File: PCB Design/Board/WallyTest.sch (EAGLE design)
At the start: 5 parts, among them IC1 ESP32-S3-WROOM-1-N16

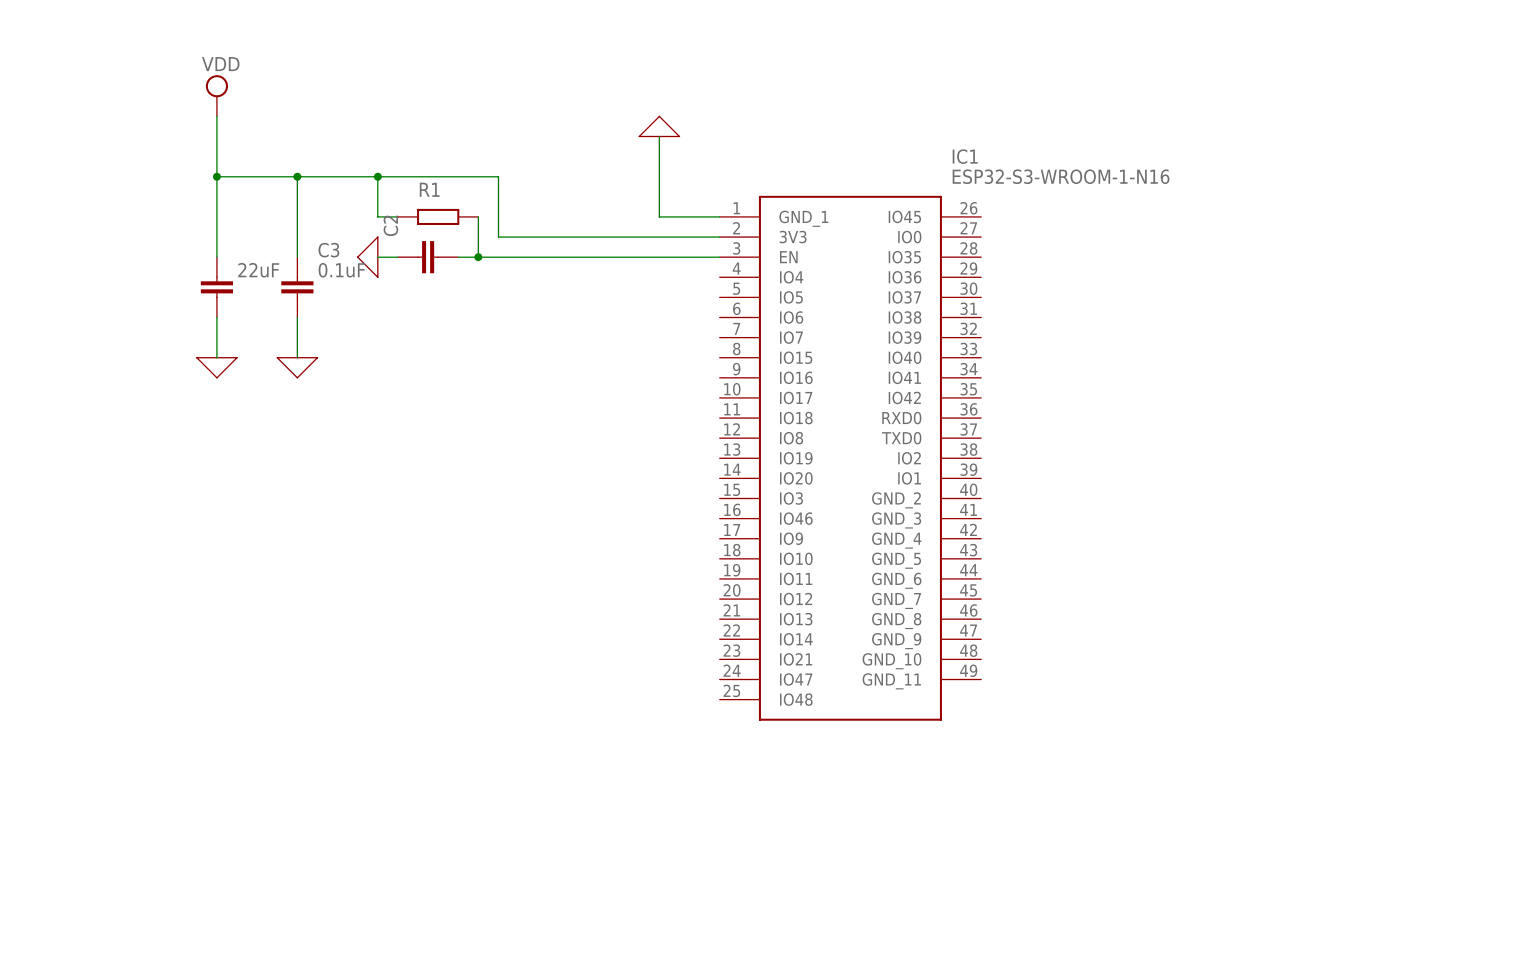
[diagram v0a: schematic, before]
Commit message: wally board with gps and lora
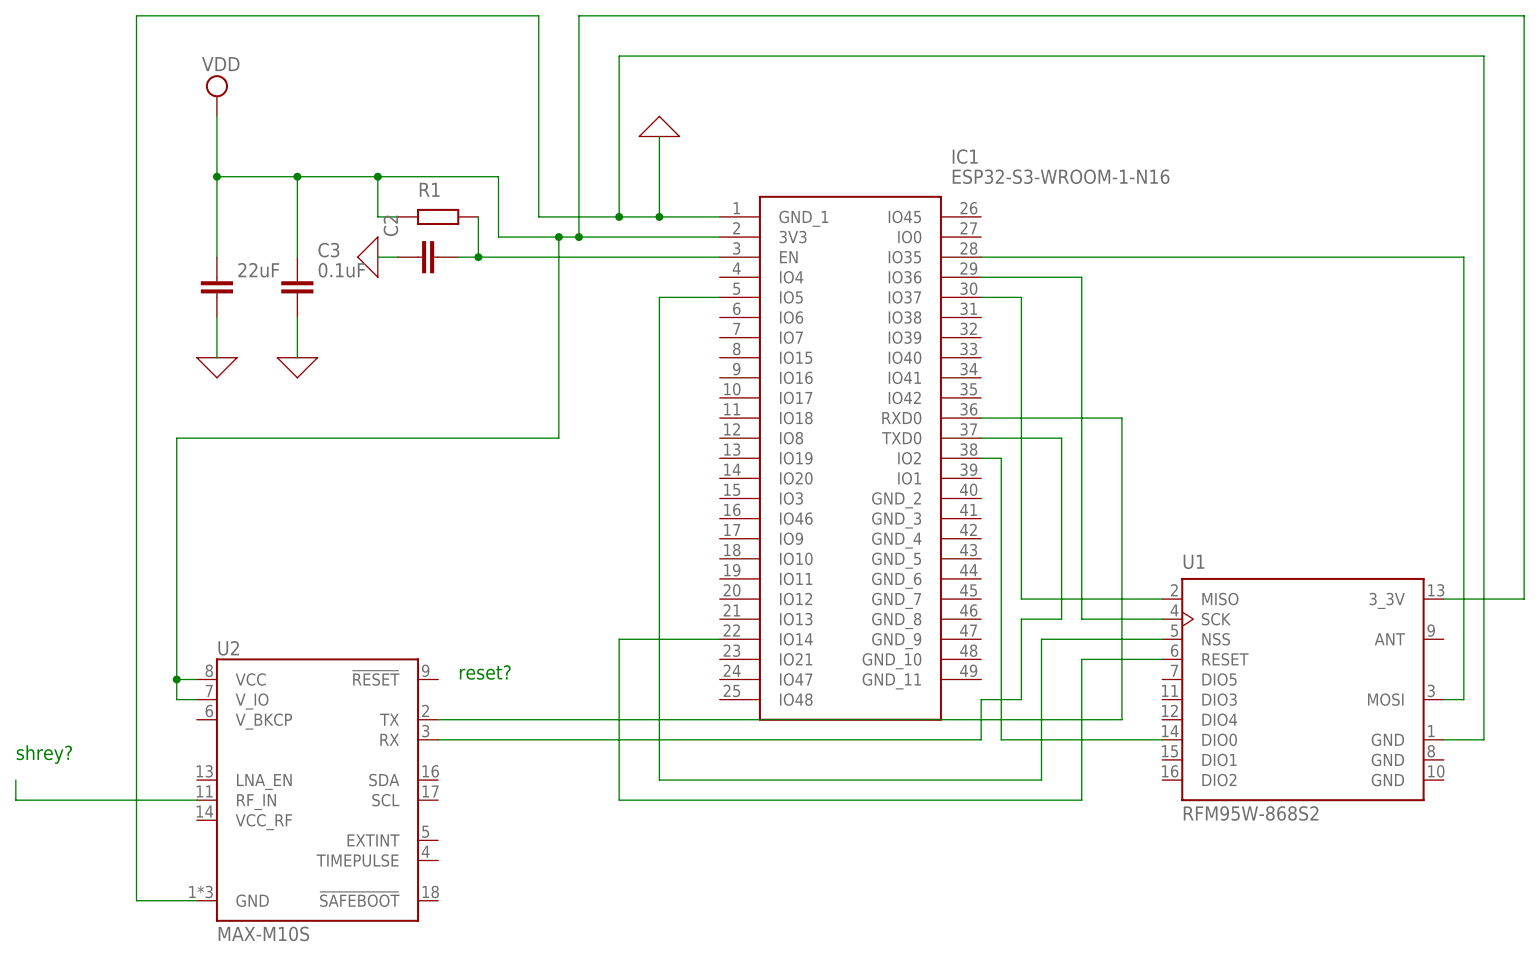
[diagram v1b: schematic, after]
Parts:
- added U1: RFM95W-868S2, RFM95W-868S2:RFM95W-868S2
- added U2: MAX-M10S, gps:MAX-M10S
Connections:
- new net N$12: U2.RF_IN
- new net N$2: IC1.IO36, U1.SCK
- new net N$3: IC1.IO35, U1.MOSI
- new net N$4: IC1.IO37, U1.MISO
- new net N$5: IC1.IO2, U1.DIO0
- new net N$6: IC1.IO5, U1.NSS
- new net N$7: IC1.IO14, U1.RESET
- new net N$8: IC1.RXD0, U2.TX
- new net N$9: IC1.TXD0, U2.RX
- net 0: now also U1.GND, U2.GND
- net VDD: now also U1.3_3V, U2.VCC, U2.V_IO
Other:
- note added: "reset?"
- note added: "shrey?"
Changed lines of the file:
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@@
 <part name="C2" library="ngspice-simulation" library_urn="urn:adsk.eagle:library:527439" deviceset="C" device=""/>
 <part name="X_4" library="ngspice-simulation" library_urn="urn:adsk.eagle:library:527439" deviceset="GND" device=""/>
+<part name="U1" library="RFM95W-868S2" deviceset="RFM95W-868S2" device=""/>
+<part name="U2" library="gps" deviceset="MAX-M10S" device=""/>
 </parts>
 <sheets>
 <sheet>
 <plain>
+<text x="33.02" y="10.16" size="1.778" layer="91">reset?</text>
+<text x="-22.86" y="0" size="1.778" layer="91">shrey?</text>
 </plain>
 <instances>
@@
 </instance>
 <instance part="X_4" gate="G$1" x="22.86" y="63.5" smashed="yes" rot="R270"/>
+<instance part="U1" gate="G$1" x="139.7" y="10.16" smashed="yes">
+<attribute name="NAME" x="124.4437" y="24.1449" size="1.7799" layer="95"/>
+<attribute name="VALUE" x="124.435" y="-7.6492" size="1.78091875" layer="96"/>
+</instance>
+<instance part="U2" gate="U1" x="15.24" y="-2.54" smashed="yes">
+<attribute name="NAME" x="2.54" y="13.208" size="1.778" layer="95"/>
+<attribute name="VALUE" x="2.54" y="-22.86" size="1.778" layer="96"/>
+</instance>
 </instances>
 <busses>
@@
 <pinref part="X_1" gate="G$1" pin="0"/>
 <wire x1="58.42" y1="68.58" x2="58.42" y2="78.74" width="0.1524" layer="91"/>
+<pinref part="U1" gate="G$1" pin="GND"/>
+<wire x1="157.48" y1="2.54" x2="162.56" y2="2.54" width="0.1524" layer="91"/>
+<wire x1="162.56" y1="2.54" x2="162.56" y2="88.9" width="0.1524" layer="91"/>
+<wire x1="162.56" y1="88.9" x2="53.34" y2="88.9" width="0.1524" layer="91"/>
+<wire x1="53.34" y1="88.9" x2="53.34" y2="68.58" width="0.1524" layer="91"/>
+<wire x1="53.34" y1="68.58" x2="58.42" y2="68.58" width="0.1524" layer="91"/>
+<junction x="58.42" y="68.58"/>
+<pinref part="U2" gate="U1" pin="GND"/>
+<wire x1="0" y1="-17.78" x2="-7.62" y2="-17.78" width="0.1524" layer="91"/>
+<wire x1="-7.62" y1="-17.78" x2="-7.62" y2="93.98" width="0.1524" layer="91"/>
+<wire x1="-7.62" y1="93.98" x2="43.18" y2="93.98" width="0.1524" layer="91"/>
+<wire x1="43.18" y1="93.98" x2="43.18" y2="68.58" width="0.1524" layer="91"/>
+<wire x1="43.18" y1="68.58" x2="53.34" y2="68.58" width="0.1524" layer="91"/>
+<junction x="53.34" y="68.58"/>
 </segment>
 <segment>
@@
 <segment>
 <pinref part="IC1" gate="G$1" pin="3V3"/>
-<wire x1="66.04" y1="66.04" x2="38.1" y2="66.04" width="0.1524" layer="91"/>
+<wire x1="66.04" y1="66.04" x2="48.26" y2="66.04" width="0.1524" layer="91"/>
+<wire x1="48.26" y1="66.04" x2="45.72" y2="66.04" width="0.1524" layer="91"/>
+<wire x1="45.72" y1="66.04" x2="38.1" y2="66.04" width="0.1524" layer="91"/>
 <wire x1="38.1" y1="66.04" x2="38.1" y2="73.66" width="0.1524" layer="91"/>
 <wire x1="38.1" y1="73.66" x2="22.86" y2="73.66" width="0.1524" layer="91"/>
@@
 <pinref part="R1" gate="G$1" pin="1"/>
 <wire x1="22.86" y1="68.58" x2="25.4" y2="68.58" width="0.1524" layer="91"/>
+<pinref part="U1" gate="G$1" pin="3_3V"/>
+<wire x1="157.48" y1="20.32" x2="167.64" y2="20.32" width="0.1524" layer="91"/>
+<wire x1="167.64" y1="20.32" x2="167.64" y2="93.98" width="0.1524" layer="91"/>
+<wire x1="167.64" y1="93.98" x2="48.26" y2="93.98" width="0.1524" layer="91"/>
+<wire x1="48.26" y1="93.98" x2="48.26" y2="66.04" width="0.1524" layer="91"/>
+<junction x="48.26" y="66.04"/>
+<pinref part="U2" gate="U1" pin="VCC"/>
+<wire x1="0" y1="10.16" x2="-2.54" y2="10.16" width="0.1524" layer="91"/>
+<wire x1="-2.54" y1="10.16" x2="-2.54" y2="40.64" width="0.1524" layer="91"/>
+<wire x1="-2.54" y1="40.64" x2="45.72" y2="40.64" width="0.1524" layer="91"/>
+<wire x1="45.72" y1="40.64" x2="45.72" y2="66.04" width="0.1524" layer="91"/>
+<junction x="45.72" y="66.04"/>
+<pinref part="U2" gate="U1" pin="V_IO"/>
+<wire x1="0" y1="7.62" x2="-2.54" y2="7.62" width="0.1524" layer="91"/>
+<wire x1="-2.54" y1="7.62" x2="-2.54" y2="10.16" width="0.1524" layer="91"/>
+<junction x="-2.54" y="10.16"/>
 </segment>
 </net>
@@
 </segment>
 </net>
+<net name="N$3" class="0">
+<segment>
+<pinref part="U1" gate="G$1" pin="MOSI"/>
+<wire x1="157.48" y1="7.62" x2="160.02" y2="7.62" width="0.1524" layer="91"/>
+<wire x1="160.02" y1="7.62" x2="160.02" y2="63.5" width="0.1524" layer="91"/>
+<pinref part="IC1" gate="G$1" pin="IO35"/>
+<wire x1="160.02" y1="63.5" x2="99.06" y2="63.5" width="0.1524" layer="91"/>
+</segment>
+</net>
+<net name="N$2" class="0">
+<segment>
+<pinref part="U1" gate="G$1" pin="SCK"/>
+<wire x1="121.92" y1="17.78" x2="111.76" y2="17.78" width="0.1524" layer="91"/>
+<wire x1="111.76" y1="17.78" x2="111.76" y2="60.96" width="0.1524" layer="91"/>
+<pinref part="IC1" gate="G$1" pin="IO36"/>
+<wire x1="111.76" y1="60.96" x2="99.06" y2="60.96" width="0.1524" layer="91"/>
+</segment>
+</net>
+<net name="N$4" class="0">
+<segment>
+<pinref part="U1" gate="G$1" pin="MISO"/>
+<wire x1="121.92" y1="20.32" x2="104.14" y2="20.32" width="0.1524" layer="91"/>
+<wire x1="104.14" y1="20.32" x2="104.14" y2="58.42" width="0.1524" layer="91"/>
+<pinref part="IC1" gate="G$1" pin="IO37"/>
+<wire x1="104.14" y1="58.42" x2="99.06" y2="58.42" width="0.1524" layer="91"/>
+</segment>
+</net>
+<net name="N$5" class="0">
+<segment>
+<pinref part="U1" gate="G$1" pin="DIO0"/>
+<wire x1="121.92" y1="2.54" x2="101.6" y2="2.54" width="0.1524" layer="91"/>
+<pinref part="IC1" gate="G$1" pin="IO2"/>
+<wire x1="101.6" y1="2.54" x2="101.6" y2="38.1" width="0.1524" layer="91"/>
+<wire x1="101.6" y1="38.1" x2="99.06" y2="38.1" width="0.1524" layer="91"/>
+</segment>
+</net>
+<net name="N$6" class="0">
+<segment>
+<pinref part="U1" gate="G$1" pin="NSS"/>
+<wire x1="121.92" y1="15.24" x2="106.68" y2="15.24" width="0.1524" layer="91"/>
+<wire x1="106.68" y1="15.24" x2="106.68" y2="-2.54" width="0.1524" layer="91"/>
+<wire x1="106.68" y1="-2.54" x2="58.42" y2="-2.54" width="0.1524" layer="91"/>
+<pinref part="IC1" gate="G$1" pin="IO5"/>
+<wire x1="58.42" y1="-2.54" x2="58.42" y2="58.42" width="0.1524" layer="91"/>
+<wire x1="58.42" y1="58.42" x2="66.04" y2="58.42" width="0.1524" layer="91"/>
+</segment>
+</net>
+<net name="N$7" class="0">
+<segment>
+<pinref part="U1" gate="G$1" pin="RESET"/>
+<wire x1="121.92" y1="12.7" x2="111.76" y2="12.7" width="0.1524" layer="91"/>
+<wire x1="111.76" y1="12.7" x2="111.76" y2="-5.08" width="0.1524" layer="91"/>
+<wire x1="111.76" y1="-5.08" x2="53.34" y2="-5.08" width="0.1524" layer="91"/>
+<wire x1="53.34" y1="-5.08" x2="53.34" y2="15.24" width="0.1524" layer="91"/>
+<pinref part="IC1" gate="G$1" pin="IO14"/>
+<wire x1="53.34" y1="15.24" x2="66.04" y2="15.24" width="0.1524" layer="91"/>
+</segment>
+</net>
+<net name="N$8" class="0">
+<segment>
+<pinref part="U2" gate="U1" pin="TX"/>
+<wire x1="30.48" y1="5.08" x2="116.84" y2="5.08" width="0.1524" layer="91"/>
+<wire x1="116.84" y1="5.08" x2="116.84" y2="43.18" width="0.1524" layer="91"/>
+<pinref part="IC1" gate="G$1" pin="RXD0"/>
+<wire x1="116.84" y1="43.18" x2="99.06" y2="43.18" width="0.1524" layer="91"/>
+</segment>
+</net>
+<net name="N$9" class="0">
+<segment>
+<pinref part="U2" gate="U1" pin="RX"/>
+<wire x1="30.48" y1="2.54" x2="99.06" y2="2.54" width="0.1524" layer="91"/>
+<wire x1="99.06" y1="2.54" x2="99.06" y2="7.62" width="0.1524" layer="91"/>
+<wire x1="99.06" y1="7.62" x2="104.14" y2="7.62" width="0.1524" layer="91"/>
+<wire x1="104.14" y1="7.62" x2="104.14" y2="17.78" width="0.1524" layer="91"/>
+<wire x1="104.14" y1="17.78" x2="109.22" y2="17.78" width="0.1524" layer="91"/>
+<wire x1="109.22" y1="17.78" x2="109.22" y2="40.64" width="0.1524" layer="91"/>
+<pinref part="IC1" gate="G$1" pin="TXD0"/>
+<wire x1="109.22" y1="40.64" x2="99.06" y2="40.64" width="0.1524" layer="91"/>
+</segment>
+</net>
+<net name="N$12" class="0">
+<segment>
+<pinref part="U2" gate="U1" pin="RF_IN"/>
+<wire x1="0" y1="-5.08" x2="-22.86" y2="-5.08" width="0.1524" layer="91"/>
+<wire x1="-22.86" y1="-5.08" x2="-22.86" y2="-2.54" width="0.1524" layer="91"/>
+</segment>
+</net>
